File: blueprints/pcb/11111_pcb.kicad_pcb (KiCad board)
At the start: 2 copper layers, 292.4 x 103.6 mm, 134 parts, among them J1 TRRS_MJ-4PP-9, J2 TRRS_MJ-4PP-9, SW1 SW_Push, SW10 SW_Push, SW11 SW_Push, SW12 SW_Push, SW13 SW_Push, SW14 SW_Push, SW15 SW_Push, SW16 SW_Push, SW17 SW_Push, SW18 SW_Push, SW19 SW_Push, SW2 SW_Push, SW20 SW_Push, SW21 SW_Push, SW22 SW_Push, SW23 SW_Push, SW24 SW_Push, SW25 SW_Push, SW26 SW_Push, SW27 SW_Push, SW28 SW_Push, SW29 SW_Push, SW3 SW_Push, SW30 SW_Push, SW31 SW_Push, SW32 SW_Push, SW33 SW_Push, SW34 SW_Push, SW35 SW_Push, SW36 SW_Push, SW37 SW_Push, SW38 SW_Push, SW39 SW_Push, SW4 SW_Push, SW40 SW_Push, SW41 SW_Push, SW42 SW_Push, SW43 SW_Push, SW44 SW_Push, SW45 SW_Push, SW46 SW_Push, SW47 SW_Push, SW48 SW_Push, SW49 SW_Push, SW5 SW_Push, SW50 SW_Push, SW51 SW_Push, SW52 SW_Push, SW53 SW_Push, SW54 SW_Push, SW55 SW_Push, SW56 SW_Push, SW57 SW_Push, SW58 SW_Push, SW59 SW_Push, SW6 SW_Push, SW60 SW_Push, SW61 SW_Push, SW62 SW_Push, SW63 SW_Push, SW64 SW_Push, SW7 SW_Push, SW8 SW_Push, SW9 SW_Push

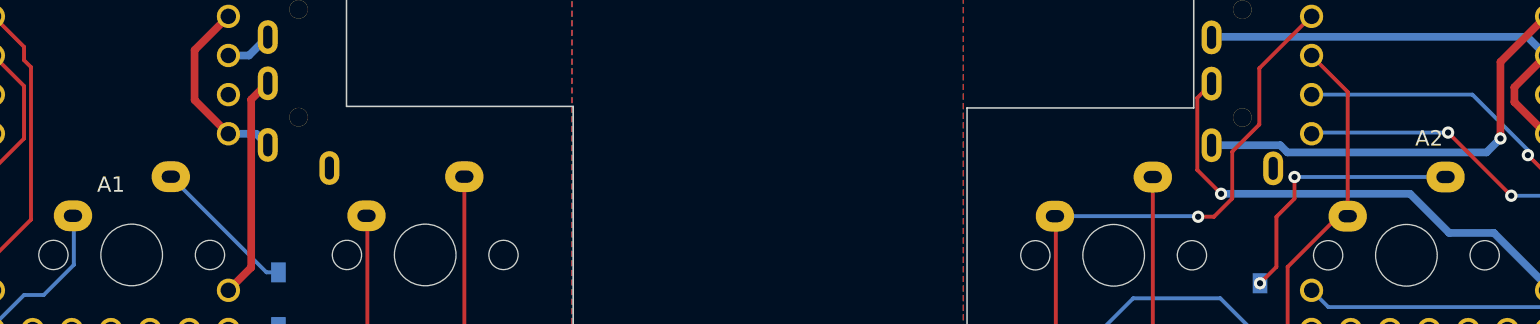
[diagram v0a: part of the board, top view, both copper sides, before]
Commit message: edit KiCad libraries
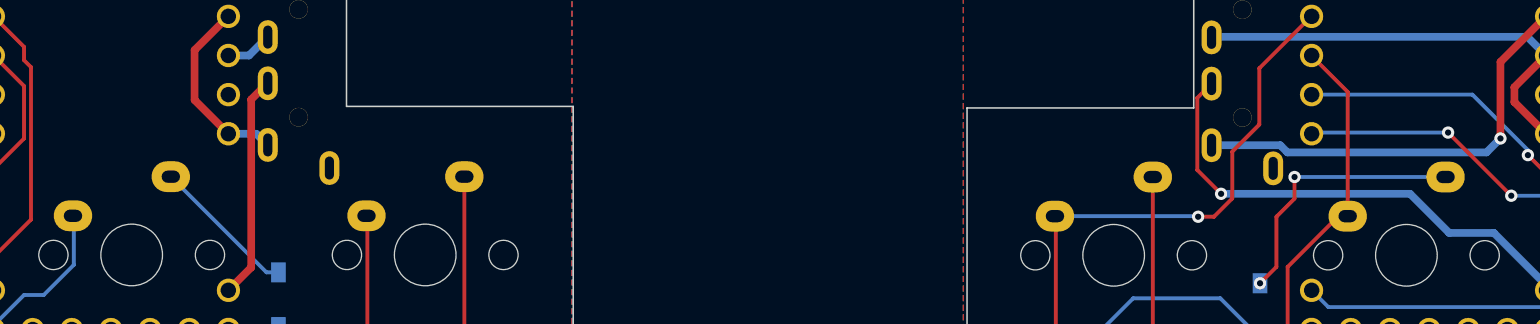
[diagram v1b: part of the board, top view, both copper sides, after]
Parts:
- A1, A2: footprint RP2040-zero:RP2040-Zero_through_hole_omit -> keyboard_parts:RP2040-Zero_reversible
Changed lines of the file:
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@@
     (property "ki_keywords" "switch normally-open pushbutton push-button")
     (attr through_hole)
-    (fp_text reference "SW9" (at -1.27 -5.08) (layer "B.SilkS")
+    (fp_text reference "SW9" (at -1.27 -7.582) (layer "B.SilkS")
         (effects (font (size 1 1) (thickness 0.15)) (justify mirror))
     )
@@
       (net 95 "Net-(D63-A)") (pinfunction "2") (pintype "passive"))
   )
-  (footprint "RP2040-zero:RP2040-Zero_through_hole_omit" (layer "B.Cu")
+  (footprint "keyboard_parts:RP2040-Zero_reversible" (layer "B.Cu")
     (at 132.6388 32.7152 180)
     (property "Sheetfile" "11111_pcb.kicad_sch")
     (property "Sheetname" "")
-    (fp_text reference "A1" (at 0 1.016 unlocked) (layer "B.SilkS")
+    (fp_text reference "A1" (at 0.5588 7.3152 unlocked) (layer "B.SilkS")
         (effects (font (size 1 1) (thickness 0.15)) (justify mirror))
     )
@@
         (effects (font (size 1 1) (thickness 0.15)) (justify mirror))
     )
-    (fp_text user "${REFERENCE}" (at 0 -0.762 unlocked) (layer "F.SilkS")
-        (effects (font (size 1 1) (thickness 0.15)))
-    )
-    (fp_text user "${REFERENCE}" (at 0 -2.54 unlocked) (layer "B.Fab")
-        (effects (font (size 1 1) (thickness 0.15)) (justify mirror))
-    )
-    (fp_text user "${REFERENCE}" (at 0 -2.5 unlocked) (layer "B.Fab")
+    (fp_text user "${REFERENCE}" (at 0.5588 7.3152 unlocked) (layer "B.Fab")
+        (effects (font (size 1 1) (thickness 0.15)) (justify mirror))
+    )
+    (fp_text user "${REFERENCE}" (at 0.5588 7.3152 unlocked) (layer "B.Fab")
         (effects (font (size 1 1) (thickness 0.15)) (justify mirror))
     )
@@
     )
   )
-  (footprint "RP2040-zero:RP2040-Zero_through_hole_omit" (layer "B.Cu")
+  (footprint "keyboard_parts:RP2040-Zero_reversible" (layer "B.Cu")
     (at 218.186 32.7152 180)
     (property "Sheetfile" "11111_pcb.kicad_sch")
     (property "Sheetname" "")
-    (fp_text reference "A2" (at 0 2.2352 unlocked) (layer "B.SilkS")
+    (fp_text reference "A2" (at 0 7.3152 unlocked) (layer "B.SilkS")
         (effects (font (size 1 1) (thickness 0.15)) (justify mirror))
     )
@@
         (effects (font (size 1 1) (thickness 0.15)) (justify mirror))
     )
-    (fp_text user "${REFERENCE}" (at 0 2.2352 unlocked) (layer "F.SilkS")
-        (effects (font (size 1 1) (thickness 0.15)))
-    )
-    (fp_text user "${REFERENCE}" (at 0 -2.54 unlocked) (layer "B.Fab")
-        (effects (font (size 1 1) (thickness 0.15)) (justify mirror))
-    )
-    (fp_text user "${REFERENCE}" (at 0 2.2352 unlocked) (layer "B.Fab")
-        (effects (font (size 1 1) (thickness 0.15)) (justify mirror))
-    )
+    (fp_text user "${REFERENCE}" (at -0.254 7.3152 unlocked) (layer "B.Fab")
+        (effects (font (size 1 1) (thickness 0.15)) (justify mirror))
+    )
+    (fp_text user "${REFERENCE}" (at 0 7.3152 unlocked) (layer "B.Fab")
+        (effects (font (size 1 1) (thickness 0.15)) (justify mirror))
+    )
